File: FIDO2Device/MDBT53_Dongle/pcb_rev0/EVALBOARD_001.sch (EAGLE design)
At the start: 41 parts, among them CN1 IF_6PIN, CN2 USB4105-GF-A, SW1 SKRPACE010, SW2 SKTADAE010, U1 MDBT53, U2 XC6206P332MR-G, U3 RV-3028-C7, X1 NX3215SA-32.768K-STD-MUA-9

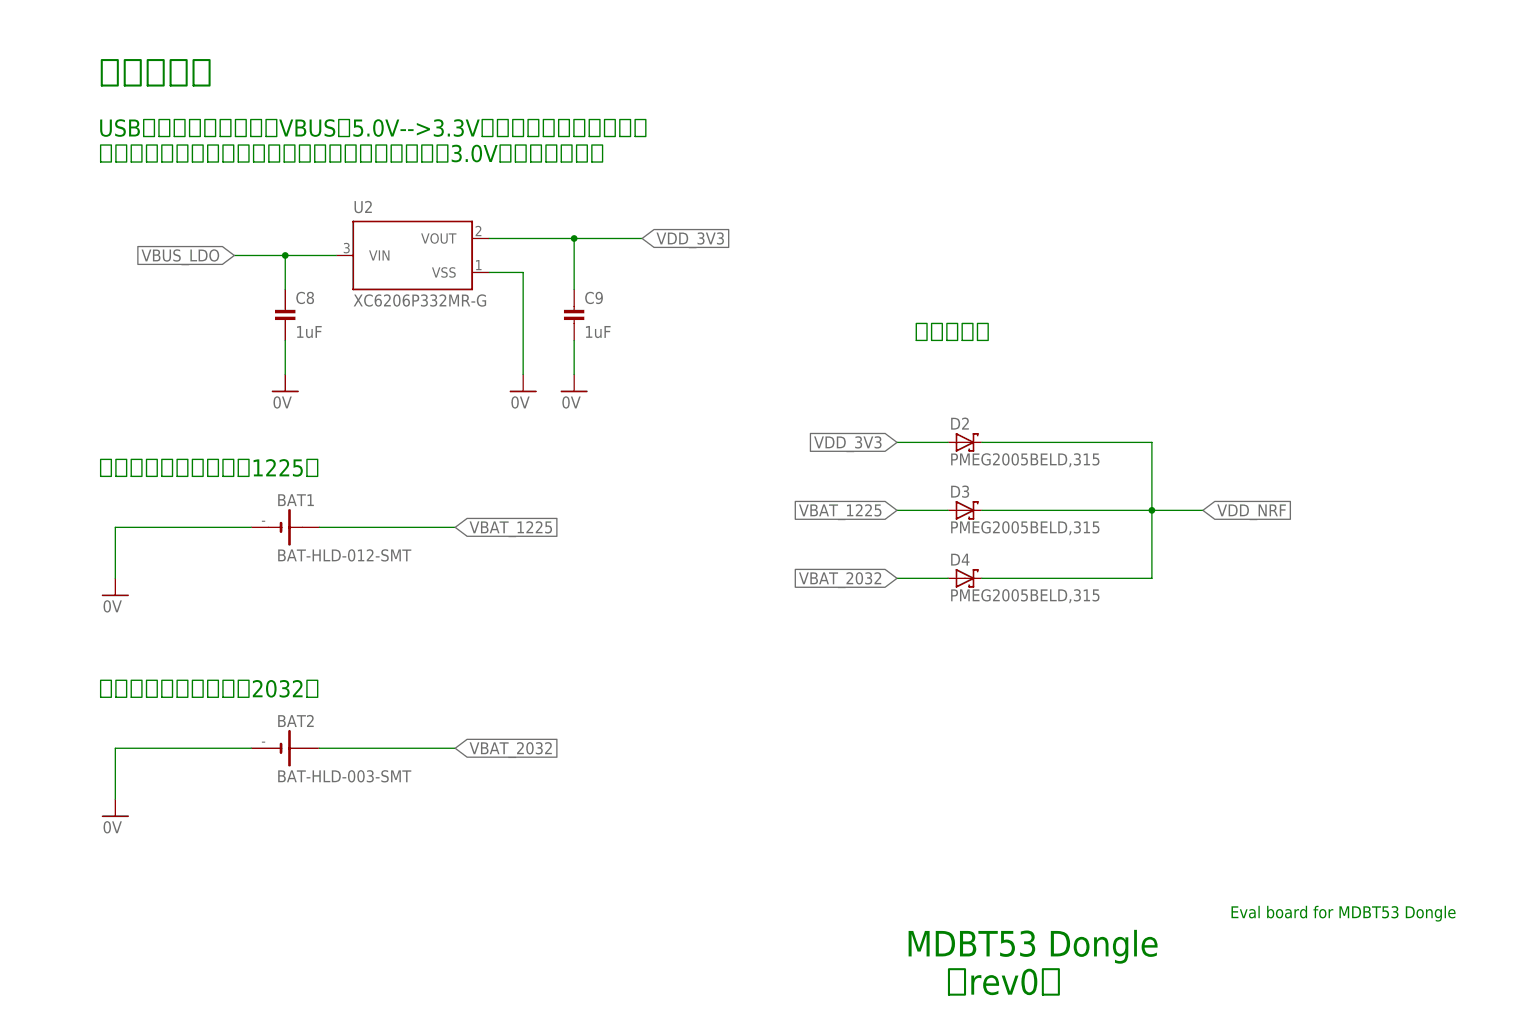
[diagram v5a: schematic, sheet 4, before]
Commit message: 回路図を作成
・ピン接続要否を検証するためのジャンパーを追加
・バイパス回路を追加
・別途検証用のスルーホールを追加
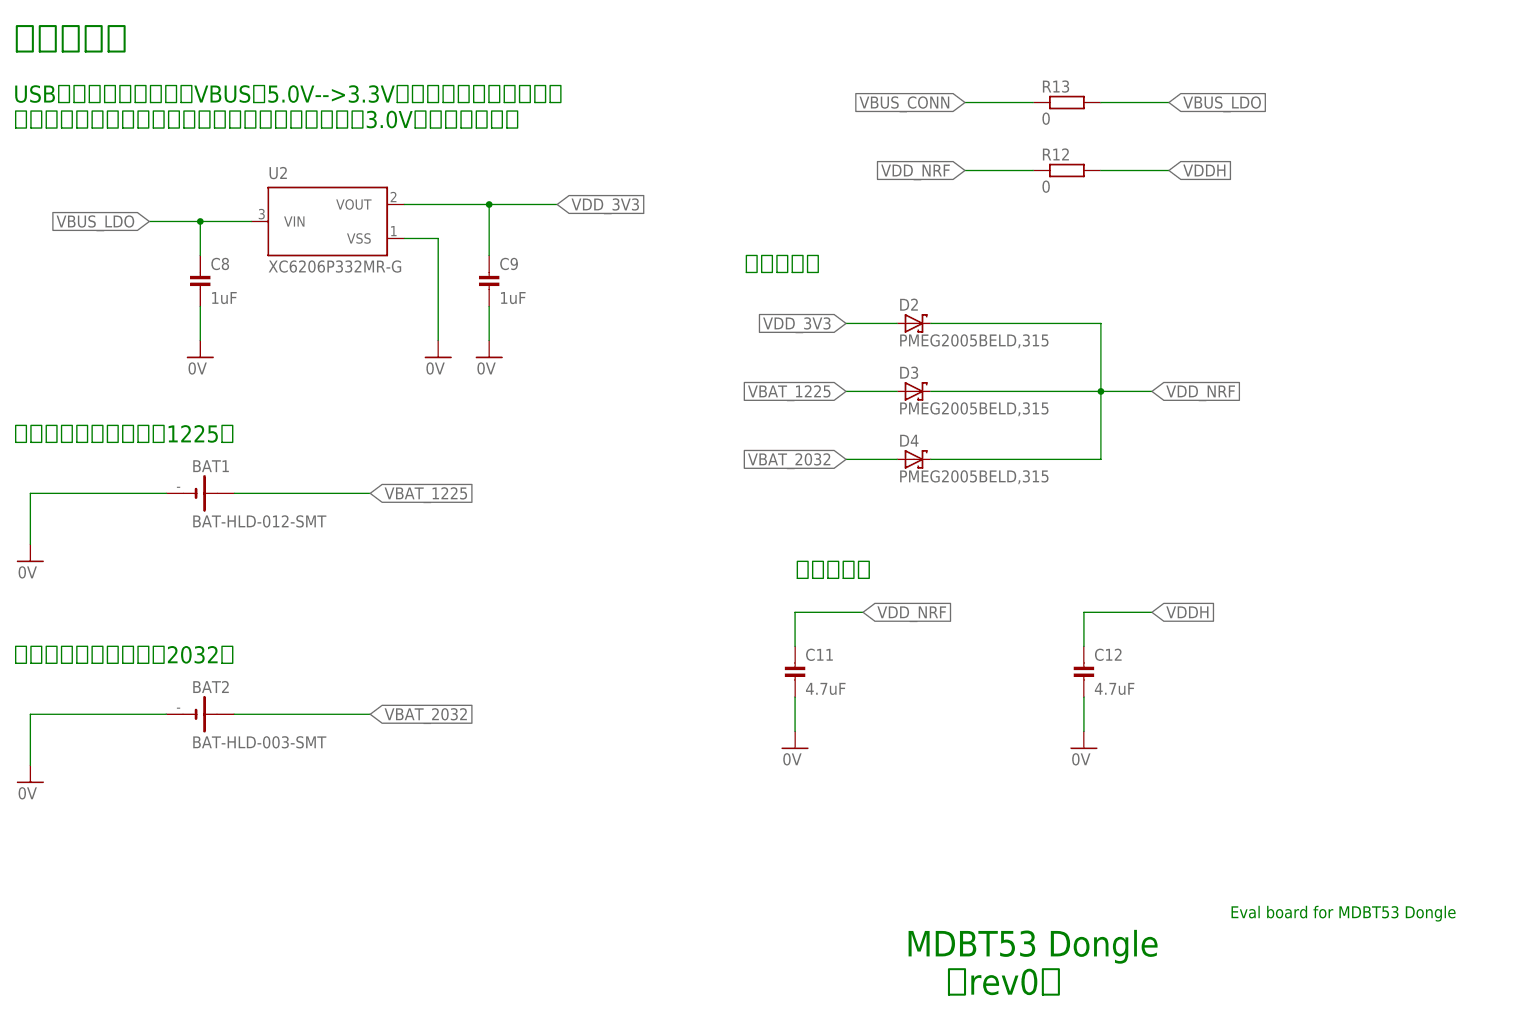
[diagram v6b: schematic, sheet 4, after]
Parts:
- removed L1: BLM15AG121SN1D, Parts:BLM15AG121SN1D
- added C10, C11, C12: 4.7uF, Parts:CAP_0603
- added CN3: IF_7PIN, Connectors:IF_7PIN
- added R11: 2.2, Parts:RESISTOR_0402
- added R12, R13: 0, Parts:RESISTOR_0603
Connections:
- net 0V: now also C10.2, C11.2, C12.2, CN3.1
- net DCC: now also CN3.3
- net DCCD: now also CN3.5
- net DCCH: now also CN3.6
- net DECD: now also CN3.4
- net DECR: now also CN3.2
- net VBUS: no longer L1.1
- net VBUS_CONN: now also R11.1, R13.1
- net VBUS_LDO: now also R13.2; no longer L1.2
- net VBUS_NRF: now also C10.1, R11.2
- net VDDH: now also C12.1, R12.2
- net VDD_NRF: now also C11.1, CN3.7, R12.1
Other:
- note added: "オプション（別途検証用）"
- note added: "バイパス用"
- moved on the sheet: BAT1, BAT2, C8, C9, D2, D3, D4, U2

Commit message: 回路図を作成
・部品番号を修正
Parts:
- removed L4: BLM15AG121SN1D, Parts:BLM15AG121SN1D
- added L1: BLM15AG121SN1D, Parts:BLM15AG121SN1D
- C10: value 4.7uF -> 1uF
- C7: value 0.1uF -> 4.7uF; device Parts:CAP_0402K -> Parts:CAP_0603
- C8: value 1uF -> 0.1uF; device Parts:CAP_0603 -> Parts:CAP_0402K
- CN1: value IF_6PIN -> USB4105-GF-A; device Connectors:IF_6PIN -> Connectors:USB4105-GF-A
- CN2: value USB4105-GF-A -> IF_6PIN; device Connectors:USB4105-GF-A -> Connectors:IF_6PIN
- R11: value 2.2 -> 10k
- R3: value 1.2k -> 2.2
- R5: value 1.8k -> 1.2k
- R6: value 390 -> 1.8k
- R7: value 10k -> 390
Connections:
- removed net VBATT: C7.1, U3.VDD
- net 0V: now also CN2.1, L2.2, R11.1; no longer CN1.1, L4.2, R9.1
- net D_N: now also CN1.D_N1, CN1.D_N2; no longer CN2.D_N1, CN2.D_N2
- net D_P: now also CN1.D_P1, CN1.D_P2; no longer CN2.D_P1, CN2.D_P2
- net FG: now also CN1.FG1, CN1.FG2, CN1.FG3, CN1.FG4, L3.1; no longer CN2.FG1, CN2.FG2, CN2.FG3, CN2.FG4, L4.1
- net LED1: now also R4.1; no longer R3.1
- net LED2: now also R5.1; no longer R4.1
- net LED3: now also R6.1; no longer R5.1
- net LED4: now also R7.1; no longer R6.1
- net N$1: now also R7.2; no longer R6.2
- net N$10: now also R10.2; no longer R9.2
- net N$2: now also CN1.CC1; no longer CN2.CC1
- net N$3: now also CN1.CC2; no longer CN2.CC2
- net N$6: now also R6.2; no longer R5.2
- net N$7: now also R5.2; no longer R4.2
- net N$8: now also R4.2; no longer R3.2
- net N$9: now also R11.2; no longer R10.2
- net RESET: now also CN2.5; no longer CN1.5
- net SCL: now also R9.1; no longer R8.1
- net SDA: now also R8.1; no longer R7.1
- net SWDCLK: now also CN2.4; no longer CN1.4
- net SWDIO: now also CN2.3; no longer CN1.3
- net TXD: now also CN2.6; no longer CN1.6
- net USB_GND: now also CN1.GND1, CN1.GND2, L2.1; no longer CN2.GND1, CN2.GND2, L3.1
- net VBUS: now also CN1.VBUS1, CN1.VBUS2, L1.1; no longer CN2.VBUS1, CN2.VBUS2, L2.1
- net VBUS_CONN: now also L1.2, R12.1, R3.1; no longer L2.2, R11.1, R13.1
- net VBUS_LDO: now also C9.1, R12.2; no longer C8.1, R13.2
- net VBUS_NRF: now also C7.1, R3.2; no longer C10.1, R11.2
- net VDDH: now also R13.2; no longer R12.2
- net VDD_3V3: now also C10.1; no longer C9.1
- net VDD_NRF: now also C8.1, CN2.2, R13.1, R9.2, U3.VDD; no longer CN1.2, R12.1, R7.2
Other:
- moved on the sheet: C9, L2, L3, R10, R12, R13, R4, R5, R6, R7, R8, R9

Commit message: 回路図を修正
・チップ抵抗（0402）のパッドサイズを修正
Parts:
- R1, R10, R11, R2, R4, R5, R6, R7, R8, R9: device Parts:RESISTOR_0402 -> Parts:RESISTOR_0402N
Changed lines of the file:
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@@
 <part name="GND12" library="Supply" deviceset="0V" device=""/>
 <part name="FRAME2" library="Generic" deviceset="A4L-LOC" device=""/>
-<part name="R5" library="Parts" deviceset="RESISTOR" device="_0402" value="1.2k"/>
-<part name="R6" library="Parts" deviceset="RESISTOR" device="_0402" value="1.8k"/>
-<part name="R7" library="Parts" deviceset="RESISTOR" device="_0402" value="390"/>
+<part name="R5" library="Parts" deviceset="RESISTOR" device="_0402N" value="1.2k"/>
+<part name="R6" library="Parts" deviceset="RESISTOR" device="_0402N" value="1.8k"/>
+<part name="R7" library="Parts" deviceset="RESISTOR" device="_0402N" value="390"/>
 <part name="LED1" library="Parts" deviceset="APTD1608" device="LSECK/J4-PF" value="APTD1608LSECK/J4-PF"/>
-<part name="R4" library="Parts" deviceset="RESISTOR" device="_0402" value="1.2k"/>
+<part name="R4" library="Parts" deviceset="RESISTOR" device="_0402N" value="1.2k"/>
 <part name="LED3" library="Parts" deviceset="APTD1608" device="LZGCK" value="APTD1608LZGCK"/>
 <part name="LED2" library="Parts" deviceset="APHD1608" device="LSURCK"/>
@@
 <part name="U3" library="ICs" deviceset="RV-3028-C7" device=""/>
 <part name="GND20" library="Supply" deviceset="0V" device=""/>
-<part name="R8" library="Parts" deviceset="RESISTOR" device="_0402" value="10k"/>
-<part name="R9" library="Parts" deviceset="RESISTOR" device="_0402" value="10k"/>
-<part name="R10" library="Parts" deviceset="RESISTOR" device="_0402" value="10k"/>
+<part name="R8" library="Parts" deviceset="RESISTOR" device="_0402N" value="10k"/>
+<part name="R9" library="Parts" deviceset="RESISTOR" device="_0402N" value="10k"/>
+<part name="R10" library="Parts" deviceset="RESISTOR" device="_0402N" value="10k"/>
 <part name="C8" library="Parts" deviceset="CAP" device="_0402K" value="0.1uF"/>
-<part name="R11" library="Parts" deviceset="RESISTOR" device="_0402" value="10k"/>
+<part name="R11" library="Parts" deviceset="RESISTOR" device="_0402N" value="10k"/>
 <part name="FRAME3" library="Generic" deviceset="A4L-LOC" device=""/>
 <part name="L1" library="Parts" deviceset="BLM15AG" device="121SN1D"/>
@@
 <part name="L3" library="Parts" deviceset="BLM15AG" device="121SN1D"/>
 <part name="D1" library="Parts" deviceset="PRTR5V0U2X" device=""/>
-<part name="R1" library="Parts" deviceset="RESISTOR" device="_0402" value="5.1k"/>
+<part name="R1" library="Parts" deviceset="RESISTOR" device="_0402N" value="5.1k"/>
 <part name="CN1" library="Connectors" deviceset="USB4105-GF-A" device=""/>
-<part name="R2" library="Parts" deviceset="RESISTOR" device="_0402" value="5.1k"/>
+<part name="R2" library="Parts" deviceset="RESISTOR" device="_0402N" value="5.1k"/>
 <part name="GND15" library="Supply" deviceset="0V" device=""/>
 <part name="CN2" library="Connectors" deviceset="IF_6PIN" device=""/>
